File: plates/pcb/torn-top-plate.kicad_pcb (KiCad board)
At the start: 2 copper layers, 138.3 x 102.5 mm, 27 parts, among them SW2 KEY_SWITCH

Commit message: Update silkscreen
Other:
- board text added: "JLCJLCJLCJLC"

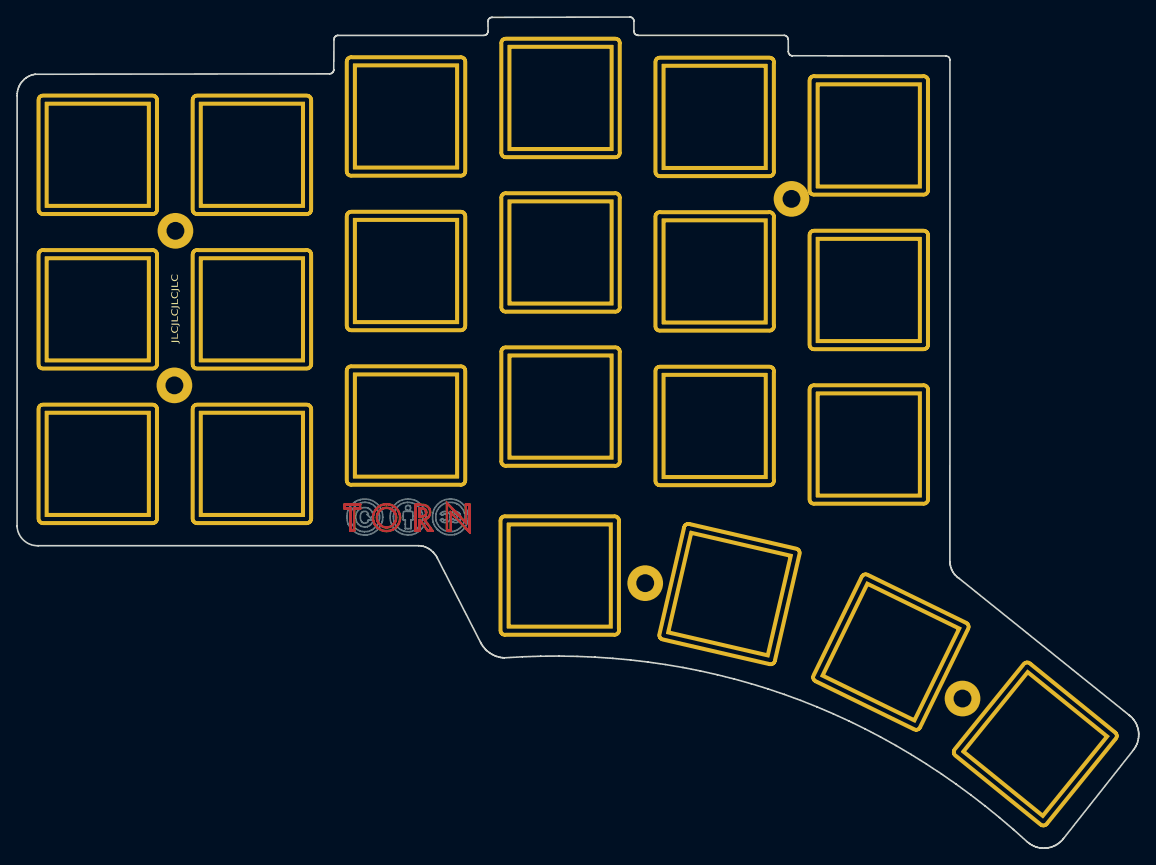
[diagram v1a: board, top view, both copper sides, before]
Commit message: Fix plate for jlcpcb
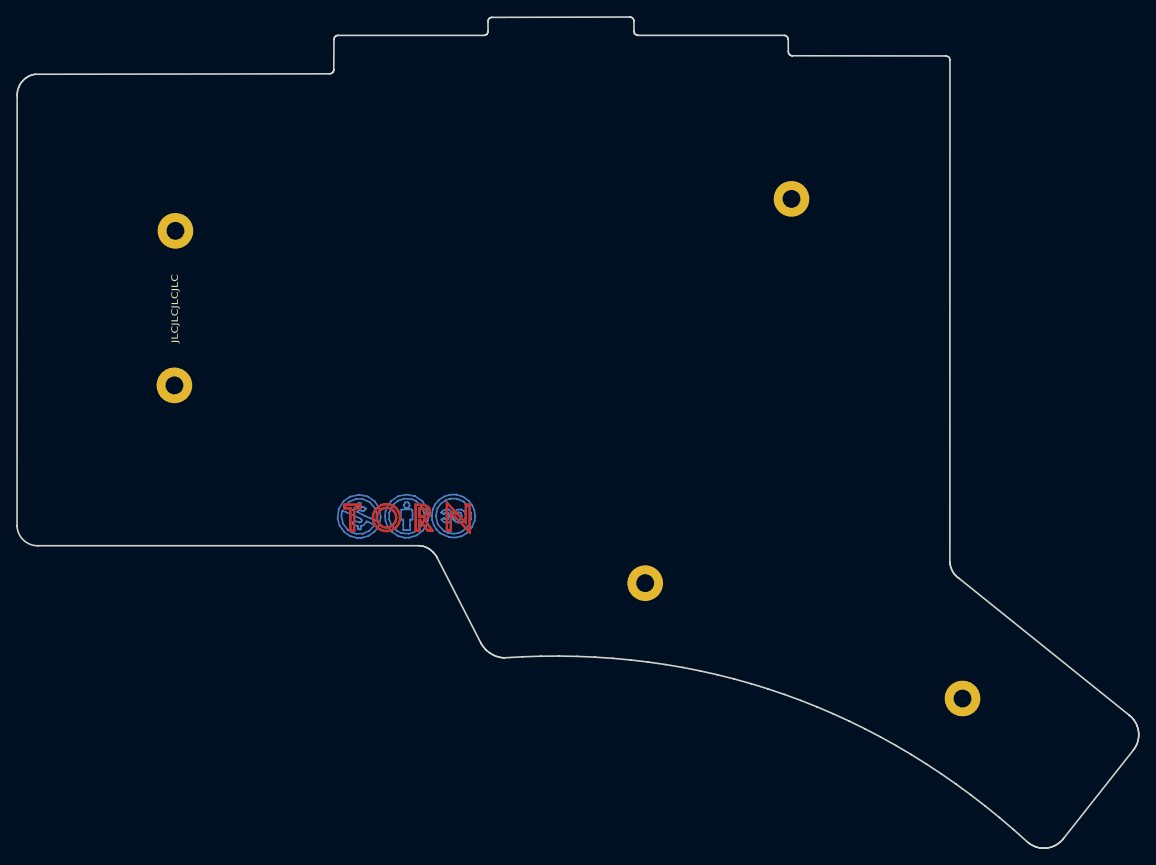
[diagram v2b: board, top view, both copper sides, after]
